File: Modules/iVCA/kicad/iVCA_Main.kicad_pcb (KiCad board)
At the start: 2 copper layers, 19.5 x 108.6 mm, 40 parts, among them Q1 BCM847BS, Q2 BCM847BS, U1 TL074, U2 TL074

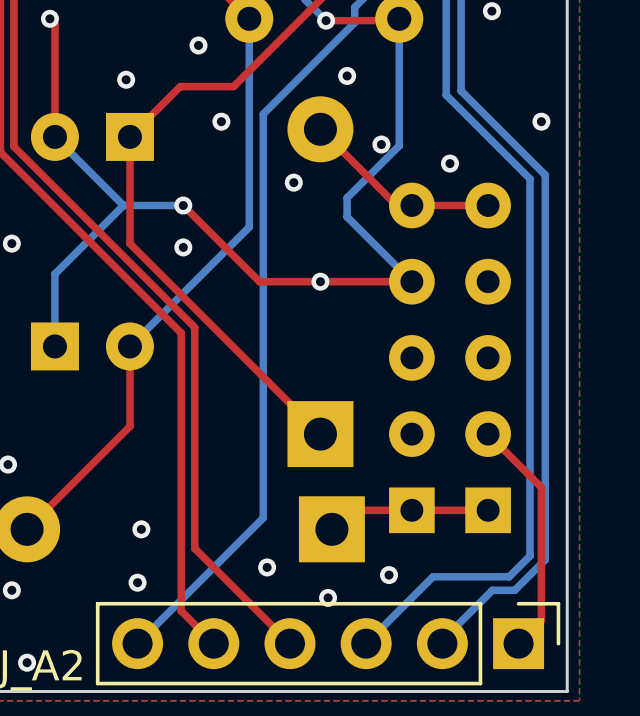
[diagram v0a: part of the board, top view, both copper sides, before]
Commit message: Add Interactive BOMs, resave all PCBs, move VU to THT.
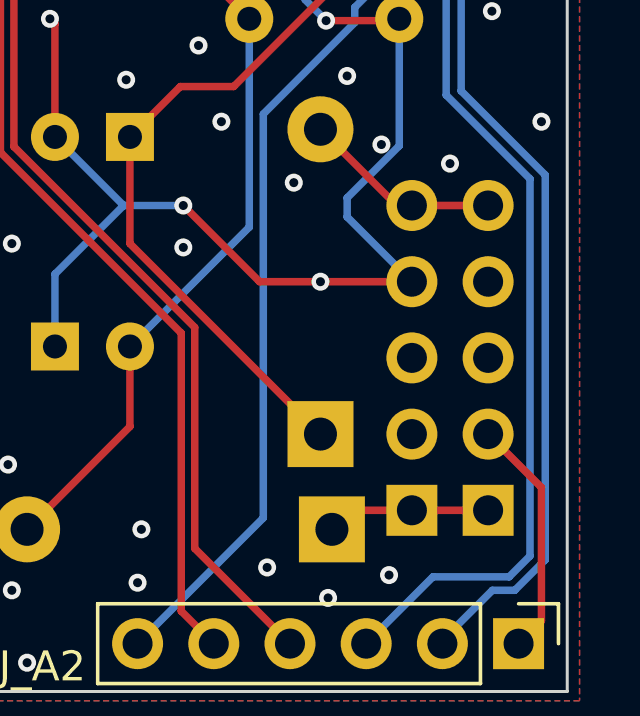
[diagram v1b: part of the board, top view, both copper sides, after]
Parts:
- R11, R12, R13, R14: value 10k -> 10k 1%
- R5, R6, R7, R8: value 20k (0.1%) -> 20k 0.1%
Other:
- board text added: "iVCA v1.4"
- board text removed: "iVCA v1.3"
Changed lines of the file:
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@@
 	)
 	(paper "A4")
+	(title_block
+		(rev "v1.4")
+	)
 	(layers
 		(0 "F.Cu" signal)
@@
 			)
 		)
-		(property "Value" "10k"
+		(property "Value" "10k 1%"
 			(at 1.27 -2.37 90)
 			(layer "B.Fab")
@@
 			)
 		)
-		(property "Value" "10k"
+		(property "Value" "10k 1%"
 			(at 1.27 -2.37 90)
 			(layer "B.Fab")
@@
 			)
 		)
-		(property "Value" "20k (0.1%)"
+		(property "Value" "20k 0.1%"
 			(at 1.27 -2.37 -90)
 			(layer "B.Fab")
@@
 			(layer "B.SilkS")
 		)
-		(fp_text user "PWR"
-			(at -1.8796 -2.032 -90)
+		(fp_text user "RED"
+			(at -1.905 -4.191 90)
+			(unlocked yes)
 			(layer "B.SilkS")
 			(effects
@@
 					(thickness 0.15)
 				)
-				(justify mirror)
+				(justify left mirror)
 			)
 		)
-		(fp_text user "RED"
-			(at -1.905 -4.191 90)
-			(unlocked yes)
+		(fp_text user "PWR"
+			(at -1.8796 -2.032 -90)
 			(layer "B.SilkS")
 			(effects
@@
 					(thickness 0.15)
 				)
-				(justify left mirror)
+				(justify mirror)
 			)
 		)
 		(pad "1" thru_hole circle
 			(at 0 5.08 180)
-			(size 1.524 1.524)
-			(drill 0.762)
+			(size 1.7 1.7)
+			(drill 1)
 			(layers "*.Cu" "*.Mask")
 			(remove_unused_layers no)
@@
 		(pad "1" thru_hole circle
 			(at 2.54 5.08 180)
-			(size 1.524 1.524)
-			(drill 0.762)
+			(size 1.7 1.7)
+			(drill 1)
 			(layers "*.Cu" "*.Mask")
 			(remove_unused_layers no)
@@
 		(pad "2" thru_hole circle
 			(at 0 -2.54 180)
-			(size 1.524 1.524)
-			(drill 0.762)
+			(size 1.7 1.7)
+			(drill 1)
 			(layers "*.Cu" "*.Mask")
 			(remove_unused_layers no)
@@
 		(pad "2" thru_hole circle
 			(at 0 0 180)
-			(size 1.524 1.524)
-			(drill 0.762)
+			(size 1.7 1.7)
+			(drill 1)
 			(layers "*.Cu" "*.Mask")
 			(remove_unused_layers no)
@@
 		(pad "2" thru_hole circle
 			(at 0 2.54 180)
-			(size 1.524 1.524)
-			(drill 0.762)
+			(size 1.7 1.7)
+			(drill 1)
 			(layers "*.Cu" "*.Mask")
 			(remove_unused_layers no)
@@
 		(pad "2" thru_hole circle
 			(at 2.54 -2.54 180)
-			(size 1.524 1.524)
-			(drill 0.762)
+			(size 1.7 1.7)
+			(drill 1)
 			(layers "*.Cu" "*.Mask")
 			(remove_unused_layers no)
@@
 		(pad "2" thru_hole circle
 			(at 2.54 0 180)
-			(size 1.524 1.524)
-			(drill 0.762)
+			(size 1.7 1.7)
+			(drill 1)
 			(layers "*.Cu" "*.Mask")
 			(remove_unused_layers no)
@@
 		(pad "2" thru_hole circle
 			(at 2.54 2.54 180)
-			(size 1.524 1.524)
-			(drill 0.762)
+			(size 1.7 1.7)
+			(drill 1)
 			(layers "*.Cu" "*.Mask")
 			(remove_unused_layers no)
@@
 		(pad "3" thru_hole rect
 			(at 0 -5.08 180)
-			(size 1.524 1.524)
-			(drill 0.762)
+			(size 1.7 1.7)
+			(drill 1)
 			(layers "*.Cu" "*.Mask")
 			(remove_unused_layers no)
@@
 		(pad "3" thru_hole rect
 			(at 2.54 -5.08 180)
-			(size 1.524 1.524)
-			(drill 0.762)
+			(size 1.7 1.7)
+			(drill 1)
 			(layers "*.Cu" "*.Mask")
 			(remove_unused_layers no)
@@
 			)
 		)
-		(property "Value" "10k"
+		(property "Value" "10k 1%"
 			(at 1.27 -2.37 90)
 			(layer "B.Fab")
@@
 			)
 		)
-		(property "Value" "20k (0.1%)"
+		(property "Value" "20k 0.1%"
 			(at 1.27 -2.37 -90)
 			(layer "B.Fab")
@@
 			)
 		)
-		(property "Value" "20k (0.1%)"
+		(property "Value" "20k 0.1%"
 			(at 1.27 -2.37 -90)
 			(layer "B.Fab")
@@
 			)
 		)
-		(property "Value" "20k (0.1%)"
+		(property "Value" "20k 0.1%"
 			(at 1.27 -2.37 -90)
 			(layer "B.Fab")
@@
 			)
 		)
-		(property "Value" "10k"
+		(property "Value" "10k 1%"
 			(at 1.27 -2.37 90)
 			(layer "B.Fab")
@@
 		(layer "Edge.Cuts")
 	)
-	(gr_text "iVCA\nv1.3"
+	(gr_text "iVCA\nv1.4"
 		(at 69.85 89.662 0)
 		(layer "B.SilkS")
